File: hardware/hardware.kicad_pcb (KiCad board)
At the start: 2 copper layers, 18 parts, among them Q1 AON6500, Q2 AON6500, Q3 AON6500, Q4 AON6500, Q5 AON6500, Q6 AON6500

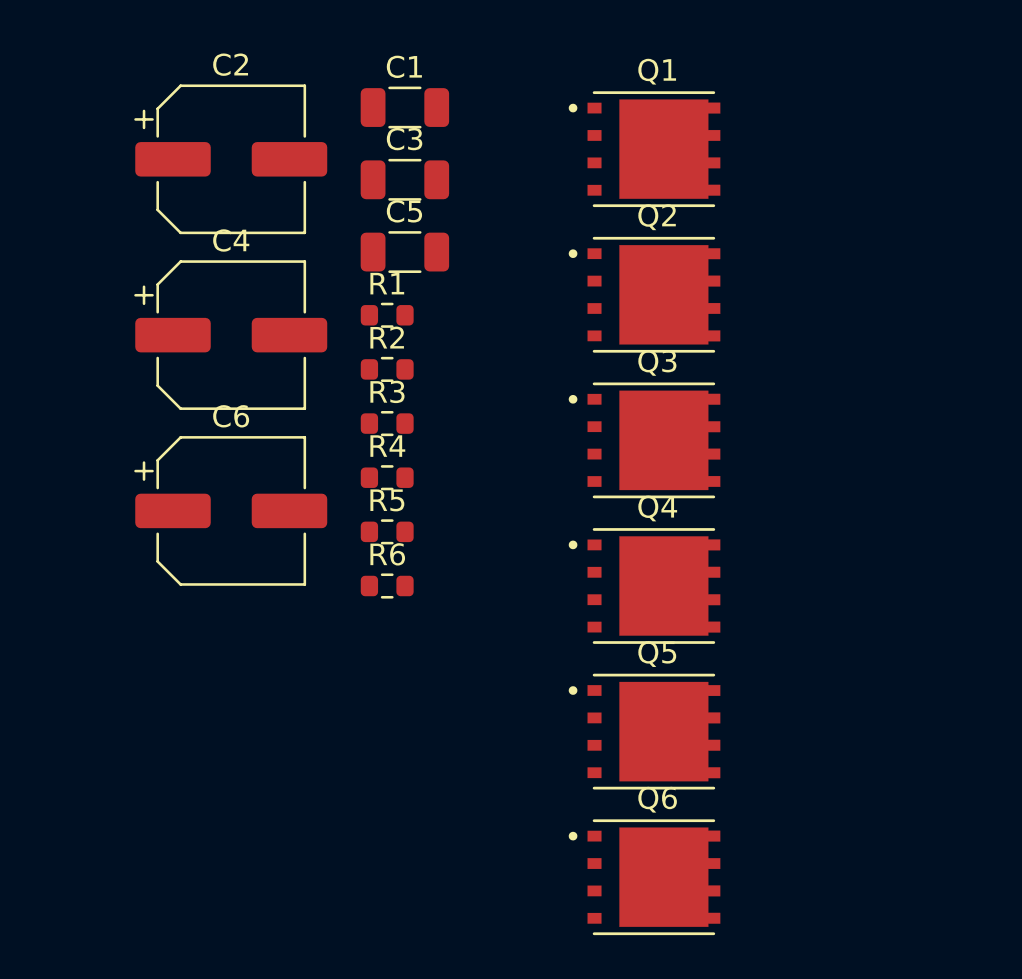
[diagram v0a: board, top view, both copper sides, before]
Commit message: add pad gnd and wire drivers with pwm
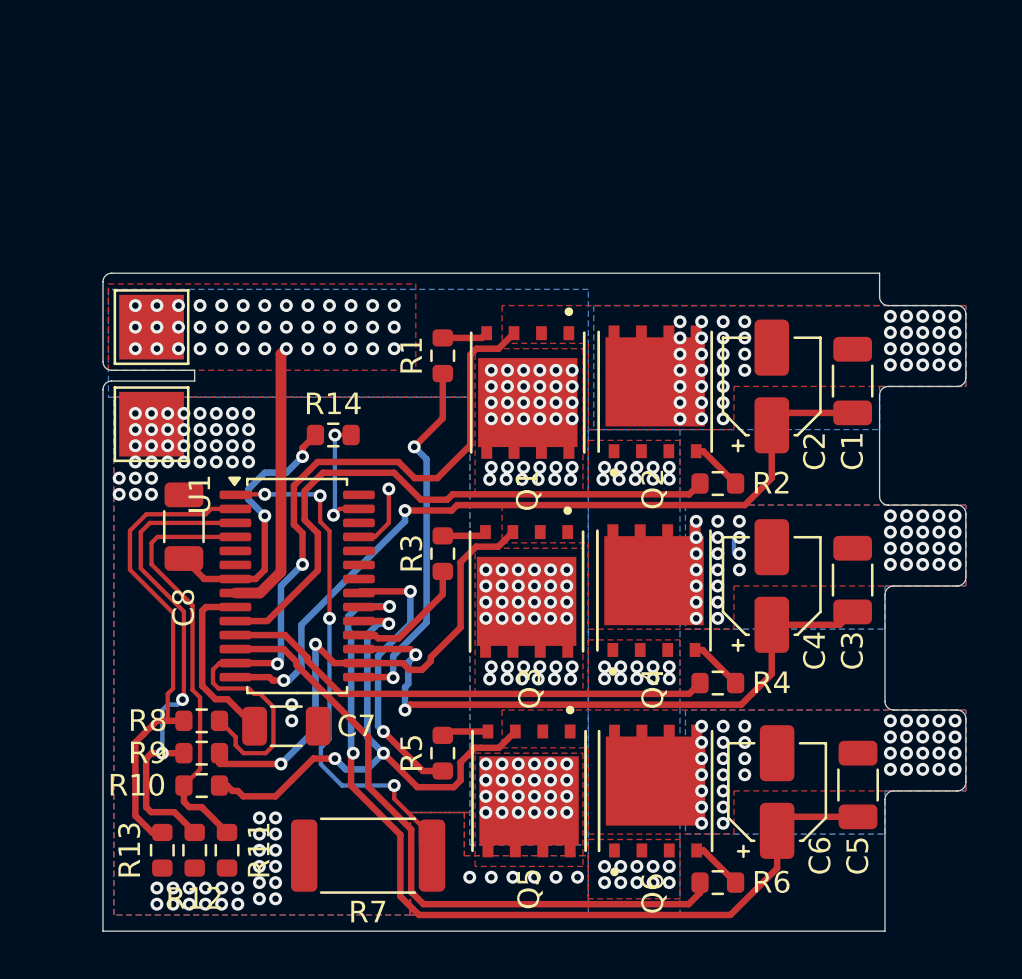
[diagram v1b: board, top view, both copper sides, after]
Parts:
- added BATT1: TestPoint_Alt, TestPoint:TestPoint_Pad_3.0x3.0mm, F.Cu at (154.8, 52.0)
- added C7: 10µF, Capacitor_SMD:C_1206_3216Metric, F.Cu at (161.0, 70.5)
- added C8: 10µF, Capacitor_SMD:C_1206_3216Metric, F.Cu at (156.2, 61.2)
- added GND1: TestPoint_Alt, TestPoint:TestPoint_Pad_3.0x3.0mm, F.Cu at (154.8, 56.5)
- added R10: 33k, Resistor_SMD:R_0603_1608Metric, F.Cu at (157.1, 73.2)
- added R11: 5.1k, Resistor_SMD:R_0603_1608Metric, F.Cu at (158.2, 76.2)
- added R12: 5.1k, Resistor_SMD:R_0603_1608Metric, F.Cu at (156.8, 76.2)
- added R13: 5.1k, Resistor_SMD:R_0603_1608Metric, F.Cu at (155.2, 76.2)
- added R14: 10k, Resistor_SMD:R_0603_1608Metric, F.Cu at (163.2, 57.0)
- added R7: 0.0005, Resistor_SMD:R_2512_6332Metric, F.Cu at (164.8, 76.5)
- added R8: 33k, Resistor_SMD:R_0603_1608Metric, F.Cu at (157.1, 70.2)
- added R9: 33k, Resistor_SMD:R_0603_1608Metric, F.Cu at (157.1, 71.8)
- added U1: CH32M007G8R6, Package_SO:TSSOP-28_4.4x9.7mm_P0.65mm, F.Cu at (161.5, 64.0)
- C2, C4, C6: footprint Capacitor_SMD:CP_Elec_6.3x3 -> Capacitor_SMD:CP_Elec_4x4.5
- R1, R2, R3, R4, R5, R6: value R -> 22
- moved C5 32.4 mm to (187.5, 73.2), turned to 90 degrees
- moved C6 28.5 mm to (183.8, 73.5), turned to 90 degrees
- moved C3 27.8 mm to (187.2, 63.7), turned to 90 degrees
- moved C4 27.6 mm to (183.5, 64.0), turned to 90 degrees
- moved C2 27.2 mm to (183.5, 54.8), turned to 90 degrees
- moved C1 24.3 mm to (187.2, 54.5), turned to 90 degrees
- moved R6 20.6 mm to (181.0, 77.8)
- moved R4 18.0 mm to (181.0, 68.5)
- moved R2 16.2 mm to (181.0, 59.2)
- moved Q1 12.7 mm to (172.2, 55.0), turned to -90 degrees
- moved R5 10.6 mm to (168.2, 71.8), turned to 90 degrees
- moved Q3 9.16 mm to (172.1, 64.3), turned to -90 degrees
- moved R3 6.56 mm to (168.2, 62.5), turned to 90 degrees
- moved Q5 6.41 mm to (172.2, 73.5), turned to -90 degrees
- moved Q2 4.50 mm to (178.1, 55.0), turned to 90 degrees
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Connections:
- net GND renamed OP1
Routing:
- net BSTW: track 0.00 -> 42.1 mm, vias 0 -> 2
- net VSU: track 0.00 -> 37.4 mm, vias 0 -> 47
- net BSTU: track 0.00 -> 36.7 mm, vias 0 -> 2
- net LGW: track 0.00 -> 30.3 mm
- net BSTV: track 0.00 -> 29.5 mm, vias 0 -> 2
- net LGU: track 0.00 -> 28.2 mm
- net VSW: track 0.00 -> 25.8 mm, vias 0 -> 41
- net OP1: track 0.00 -> 24.5 mm, vias 0 -> 40
- net VSV: track 0.00 -> 24.5 mm, vias 0 -> 40
- net PD3: track 0.00 -> 23.2 mm, vias 0 -> 2
- net LGV: track 0.00 -> 23.0 mm
- net PD2: track 0.00 -> 22.7 mm
- net PD4: track 0.00 -> 19.8 mm
- net HGU: track 0.00 -> 17.1 mm, vias 0 -> 2
- net HGW: track 0.00 -> 13.1 mm, vias 0 -> 2
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- added copper zone on B.Cu, net +BATT
- added copper zone on F.Cu, net +BATT
- added copper zone on B.Cu, net GND
- added copper zone on F.Cu, net GND
- added copper zone on B.Cu, net OP1
- added copper zone on F.Cu, net OP1
- added copper zone on B.Cu, net VSU
- added copper zone on F.Cu, net VSU
- added copper zone on B.Cu, net VSV
- added copper zone on F.Cu, net VSV
- added copper zone on B.Cu, net VSW
- added copper zone on F.Cu, net VSW
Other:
- board outline added: 40 x 30.5 mm

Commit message: finish wire pcb
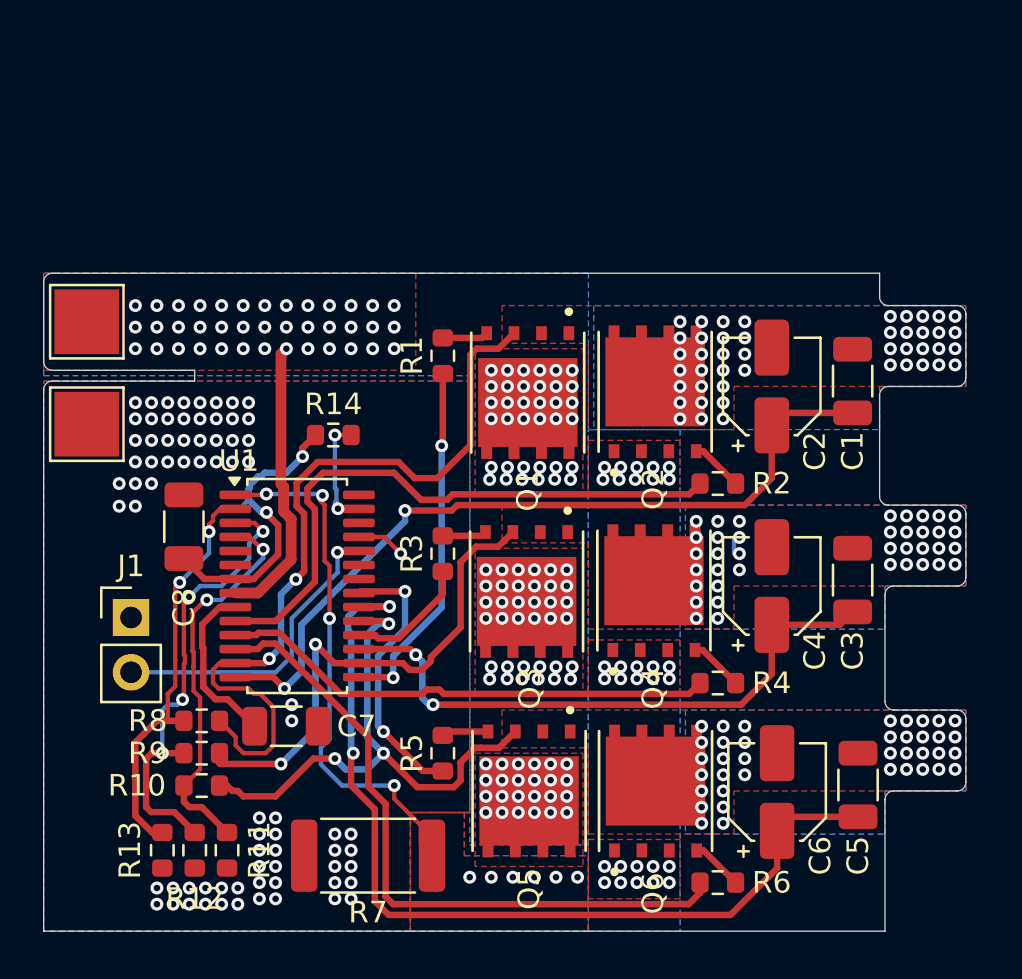
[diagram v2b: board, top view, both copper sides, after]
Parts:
- added J1: Conn_01x02, Connector_PinHeader_2.54mm:PinHeader_1x02_P2.54mm_Vertical, F.Cu at (153.8, 65.5)
- moved BATT1 3.01 mm to (151.8, 51.8)
- moved GND1 3.00 mm to (151.8, 56.5)
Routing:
- net PA1: track 0.00 -> 14.5 mm, vias 0 -> 1
- net PD2: track 22.7 -> 19.2 mm, vias 0 -> 2
- net PD4: track 19.8 -> 18.1 mm, vias 0 -> 2
- net PD3: track 23.2 -> 21.4 mm, vias 2 -> 4
- net BSTV: track 29.5 -> 28.1 mm
- net +5V: track 12.8 -> 14.0 mm
- net GND: track 3.23 -> 2.26 mm, vias 65 -> 74
- net LGW: track 30.3 -> 31.2 mm
- net BSTW: track 42.1 -> 42.9 mm
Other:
- board size 40 x 30.5 mm -> 42.8 x 30.5 mm

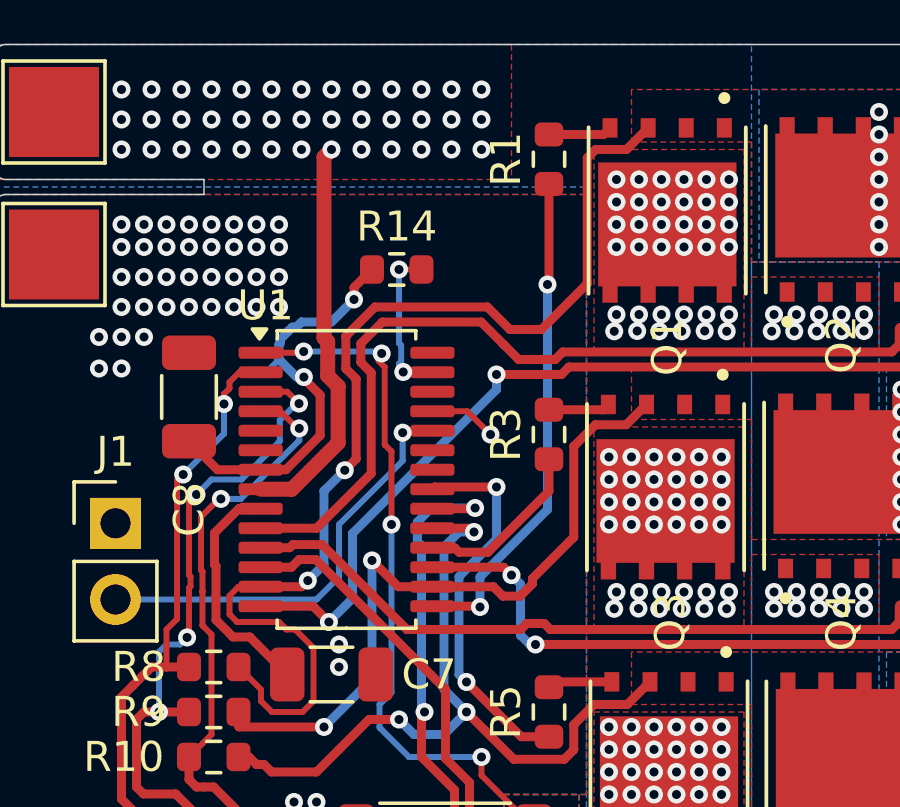
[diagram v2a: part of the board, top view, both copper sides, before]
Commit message: add programming pad
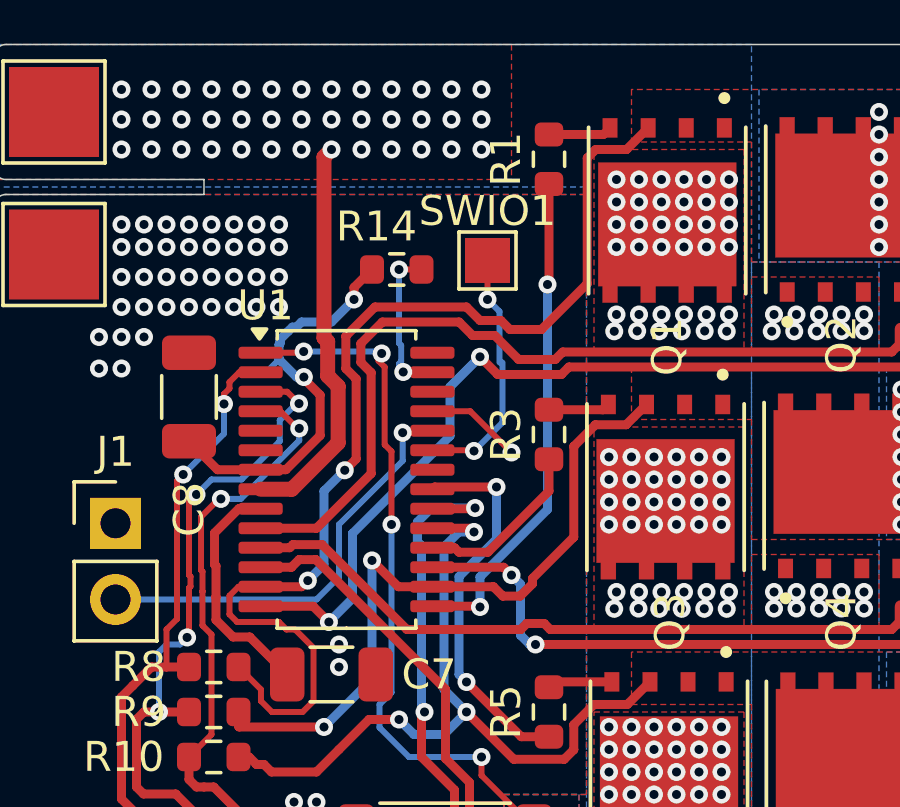
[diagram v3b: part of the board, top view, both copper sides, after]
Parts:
- added SWIO1: TestPoint_Alt, TestPoint:TestPoint_Pad_1.5x1.5mm, F.Cu at (166.2, 56.7)
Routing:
- net SWIO: track 0.00 -> 8.31 mm, vias 0 -> 2
- net BSTU: track 37.1 -> 38.3 mm
- net GND: track 2.26 -> 3.21 mm

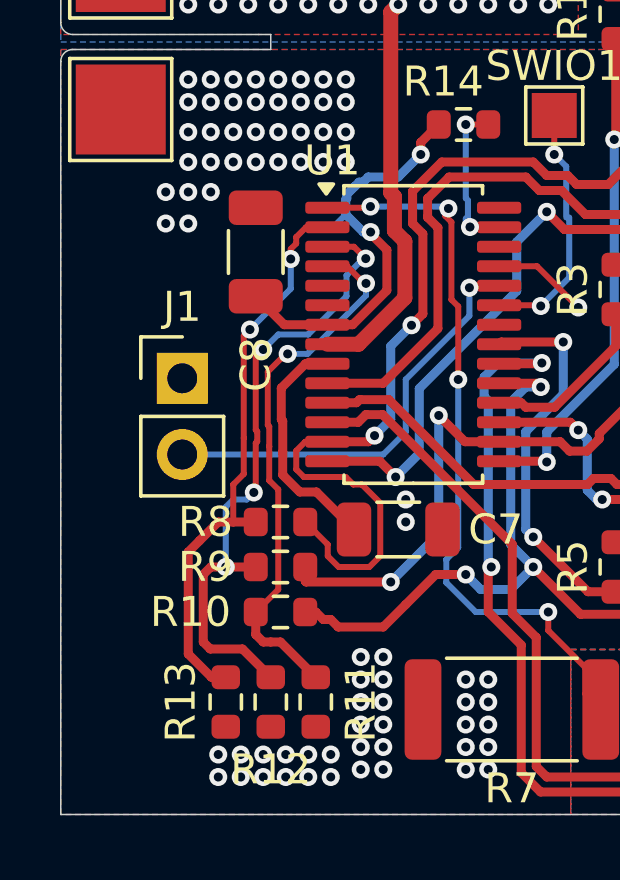
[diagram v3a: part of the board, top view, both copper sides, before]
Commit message: add 3.3v connection
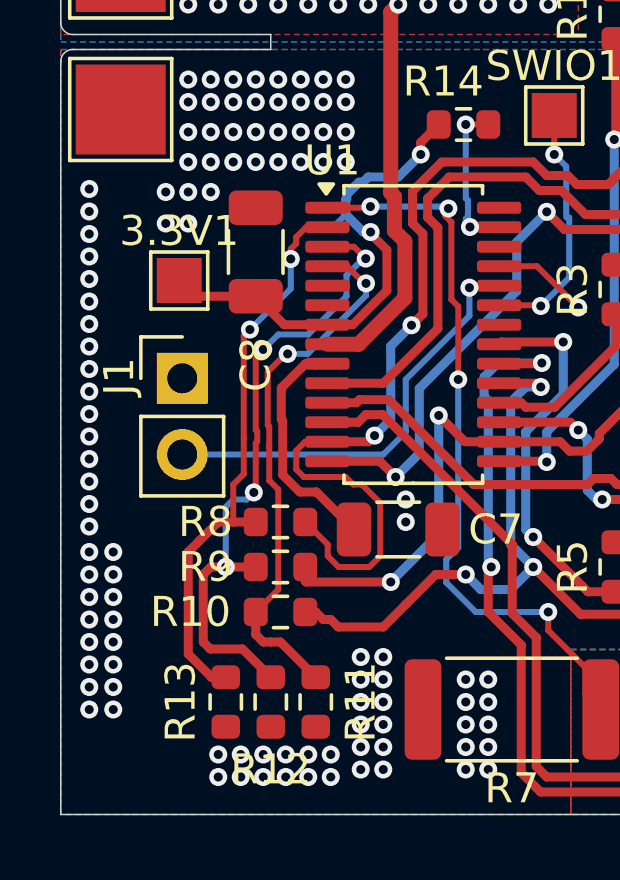
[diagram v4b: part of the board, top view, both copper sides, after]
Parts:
- added 3.3V1: TestPoint_Alt, TestPoint:TestPoint_Pad_1.5x1.5mm, F.Cu at (153.7, 62.2)
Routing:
- net +5V: track 14.0 -> 16.8 mm
- net GND: vias 74 -> 106

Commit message: add battery capacitor
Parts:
- added C10: 10µF, Capacitor_SMD:C_1206_3216Metric, F.Cu at (159.9, 54.0)
- added C11: 10µF, Capacitor_SMD:C_1206_3216Metric, F.Cu at (157.6, 54.1)
- added C9: 10µF, Capacitor_SMD:C_1206_3216Metric, F.Cu at (155.1, 54.1)

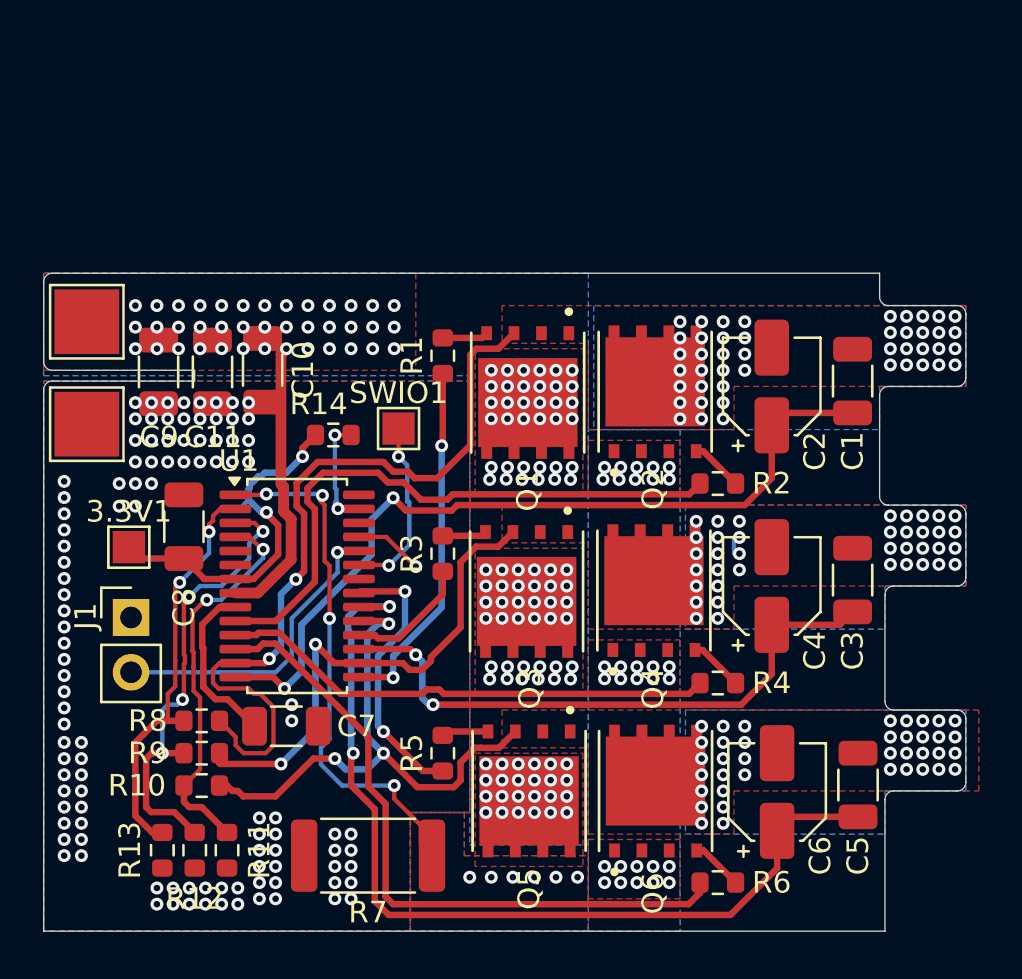
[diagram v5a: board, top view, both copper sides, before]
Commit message: update capacitor
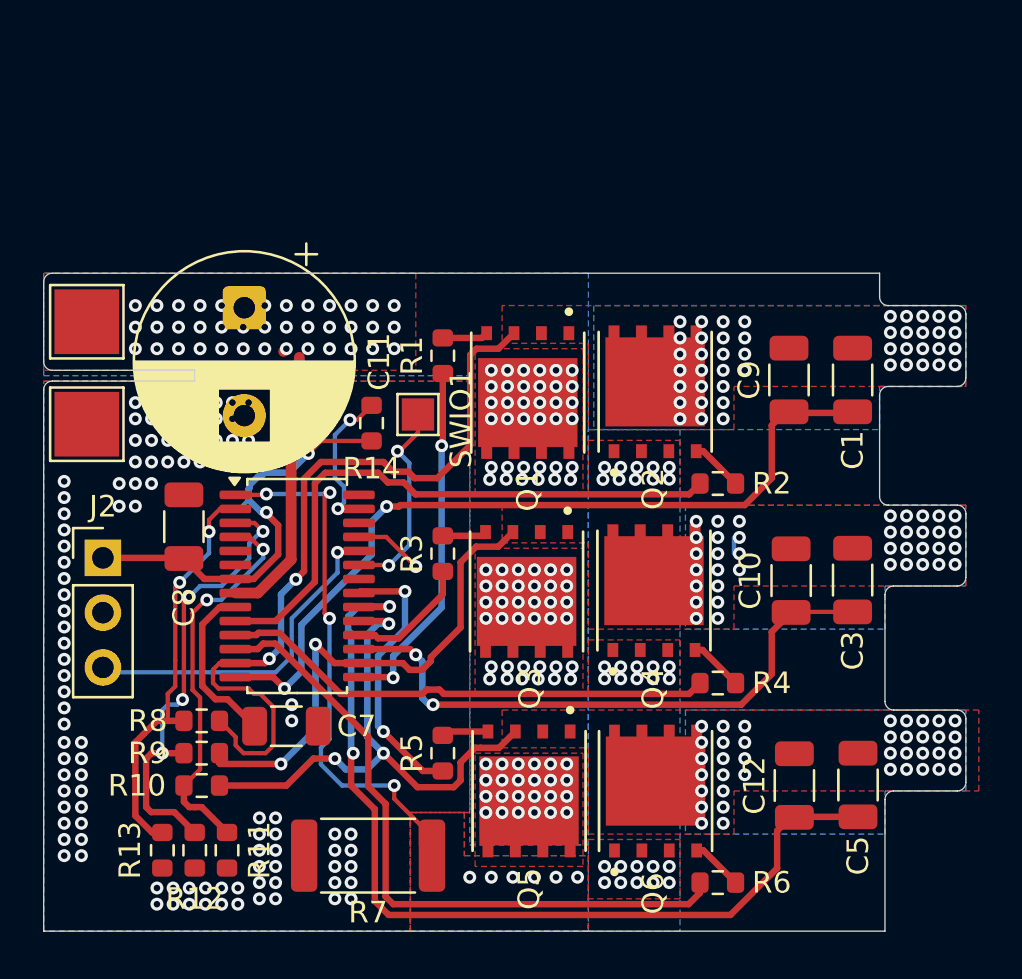
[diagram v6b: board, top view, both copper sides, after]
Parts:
- removed 3.3V1: TestPoint_Alt, TestPoint:TestPoint_Pad_1.5x1.5mm
- removed C2, C4, C6: 1µF, Capacitor_SMD:CP_Elec_4x4.5
- removed J1: Conn_01x02, Connector_PinHeader_2.54mm:PinHeader_1x02_P2.54mm_Vertical
- added C12: 2.2µF, Capacitor_SMD:C_1206_3216Metric, F.Cu at (184.6, 73.2)
- added J2: Conn_01x03, Connector_PinHeader_2.54mm:PinHeader_1x03_P2.54mm_Vertical, F.Cu at (152.5, 62.7)
- C10, C9: value 10µF -> 2.2µF
- C11: value 10µF -> 470µF; footprint Capacitor_SMD:C_1206_3216Metric -> Capacitor_THT:CP_Radial_D10.0mm_P5.00mm
- moved C9 29.2 mm to (184.3, 54.5), turned to -90 degrees
- moved C10 26.4 mm to (184.4, 63.8), turned to -90 degrees
- moved C11 3.32 mm to (159.1, 51.1), turned to -90 degrees
- moved R14 1.86 mm to (164.9, 56.5), turned to 90 degrees
- moved SWIO1 1.11 mm to (167.1, 56.0)
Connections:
- C10 pad 1: GND -> VSV
- C10 pad 2: +BATT -> BSTV
- C11 pad 1: GND -> +BATT
- C11 pad 2: +BATT -> GND
- C9 pad 1: GND -> VSU
- C9 pad 2: +BATT -> BSTU
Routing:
- net +5V: track 16.8 -> 20.1 mm
- net Net-(U1-PC5/RST/T2C1/SCL/CP0): track 5.40 -> 6.95 mm
- net PA1: track 14.5 -> 15.9 mm
- net SWIO: track 8.31 -> 9.47 mm
- net OP1: track 24.7 -> 25.3 mm
- net LGU: track 28.2 -> 27.7 mm
- net BSTU: track 38.3 -> 37.7 mm

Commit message: change gate resistors
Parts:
- R2, R4, R6: value 22 -> 15
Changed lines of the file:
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@@
 			)
 		)
-		(property "Value" "22"
+		(property "Value" "15"
 			(at 0 1.43 0)
 			(layer "F.Fab")
@@
 			)
 		)
-		(property "Value" "22"
+		(property "Value" "15"
 			(at 0 1.43 0)
 			(layer "F.Fab")
@@
 			)
 		)
-		(property "Value" "22"
+		(property "Value" "15"
 			(at 0 1.43 0)
 			(layer "F.Fab")
